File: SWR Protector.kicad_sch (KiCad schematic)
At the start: 28 parts, among them J1 Barrel_Jack, J2 Barrel_Jack, J3 transceiver, J4 antenna, J5 header, K2 ATX209, Q1 2N3904, T1 1:12, T2 1:12, U1 LM78L05_TO92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

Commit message: checkpoint changes working on V2.0
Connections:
- net +12V: now also U2.8 (V+)
- net +5V: no longer U2.8 (V+)
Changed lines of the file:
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@@
   (title_block
     (title "SWR Protector WA7GIL")
-    (date "2023-05-12")
-    (rev "v1.0")
+    (date "2023-05-27")
+    (rev "v1.1")
   )
   (junction (at 44.45 179.07) (diameter 0) (color 0 0 0 0)
@@
         (path "/5ddb5305-6e1d-4af3-a40a-20431dc1473c"
           (reference "#PWR06") (unit 1)
-        )
-      )
-    )
-  )
-  (symbol (lib_id "power:+5V") (at 129.54 161.29 0) (mirror x) (unit 1)
-    (in_bom yes) (on_board yes) (dnp no) (fields_autoplaced)
-    (property "Reference" "#PWR020" (at 129.54 157.48 0)
-      (effects (font (size 1.27 1.27)) hide)
-    )
-    (property "Value" "+5V" (at 129.54 166.37 0)
-      (effects (font (size 1.27 1.27)))
-    )
-    (property "Footprint" "" (at 129.54 161.29 0)
-      (effects (font (size 1.27 1.27)) hide)
-    )
-    (property "Datasheet" "" (at 129.54 161.29 0)
-      (effects (font (size 1.27 1.27)) hide)
-    )
-    (pin "1")
-    (instances
-      (project "SWR Protector"
-        (path "/46027dd5-036f-43c6-98e1-c4cfe473ecd7"
-          (reference "#PWR020") (unit 1)
-        )
-      )
-      (project "SWR Protector"
-        (path "/5ddb5305-6e1d-4af3-a40a-20431dc1473c"
-          (reference "#PWR020") (unit 1)
         )
       )
@@
         )
       )
+    )
+  )
+  (symbol (lib_id "power:+12V") (at 129.54 161.29 180) (unit 1)
+    (in_bom yes) (on_board yes) (dnp no) (fields_autoplaced)
+    (property "Reference" "#PWR031" (at 129.54 157.48 0)
+      (effects (font (size 1.27 1.27)) hide)
+    )
+    (property "Value" "+12V" (at 129.54 166.37 0)
+      (effects (font (size 1.27 1.27)))
+    )
+    (property "Footprint" "" (at 129.54 161.29 0)
+      (effects (font (size 1.27 1.27)) hide)
+    )
+    (property "Datasheet" "" (at 129.54 161.29 0)
+      (effects (font (size 1.27 1.27)) hide)
+    )
+    (pin "1")
+    (instances
+      (project "SWR Protector"
+        (path "/5ddb5305-6e1d-4af3-a40a-20431dc1473c"
+          (reference "#PWR031") (unit 1)
+        )
+      )

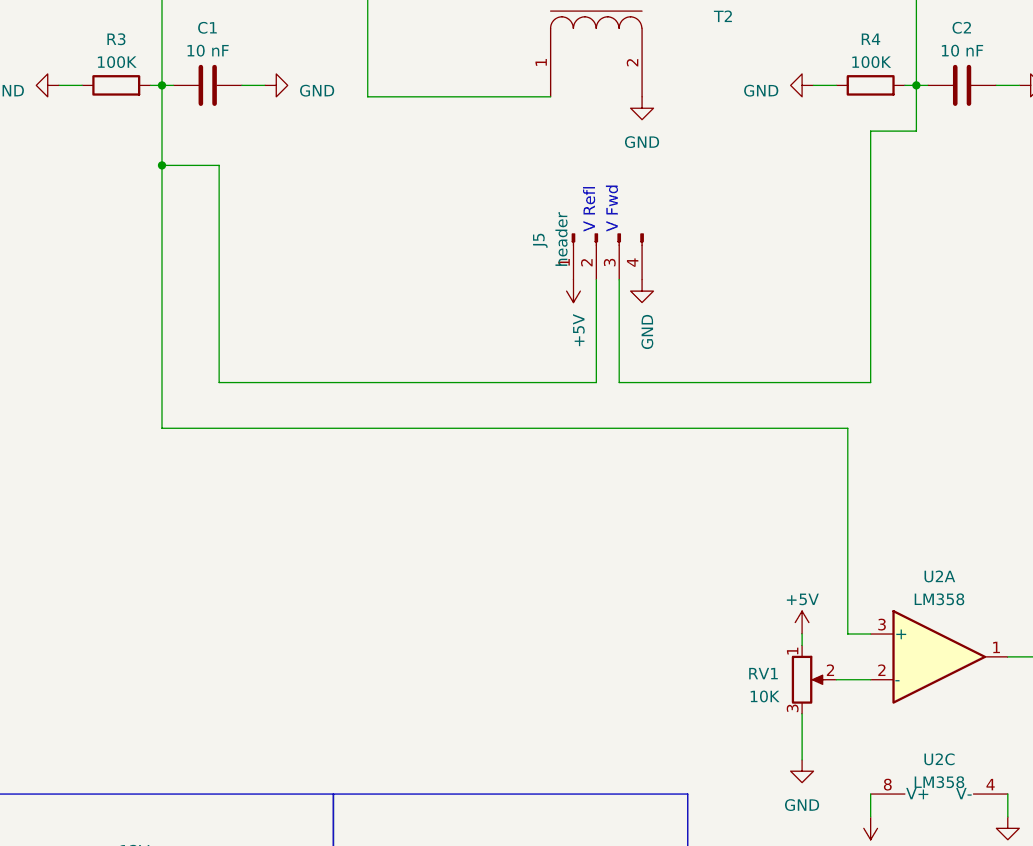
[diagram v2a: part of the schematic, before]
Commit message: v1.2 - added pins 2 & 3 from LM358 to header
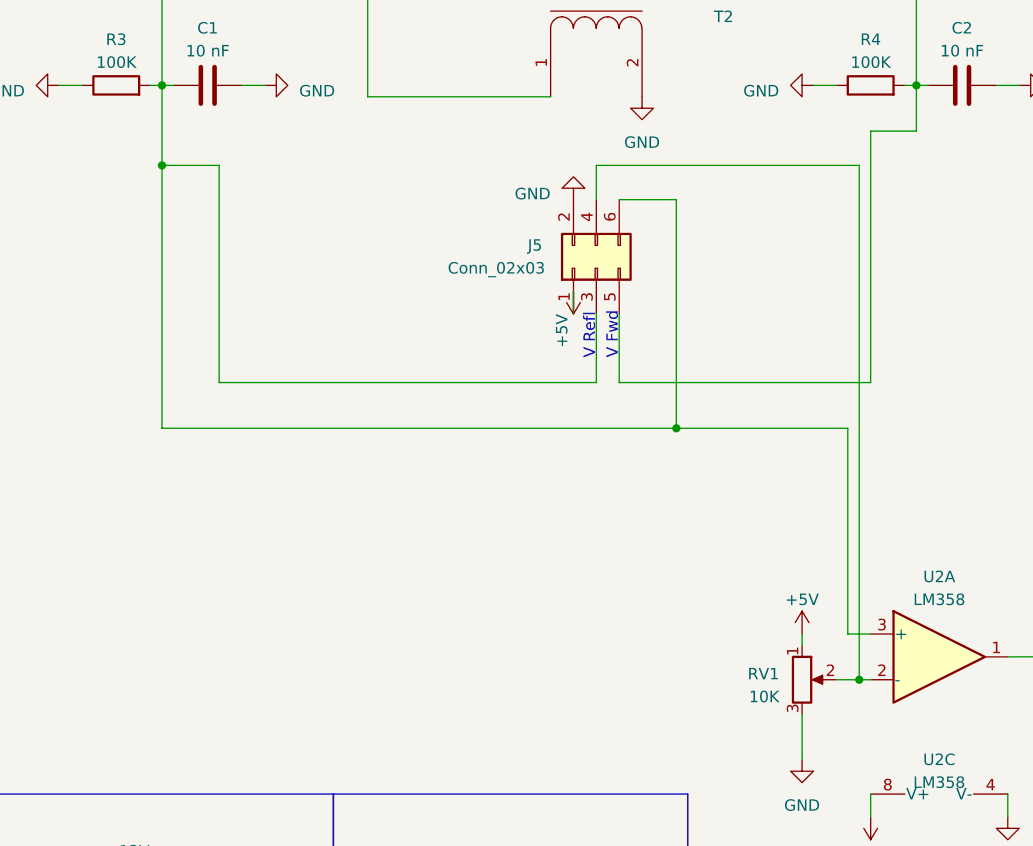
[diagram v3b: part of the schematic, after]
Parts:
- removed J5: header, Connector_PinHeader_2.54mm:PinHeader_1x04_P2.54mm_Vertical, symbol Connector:Conn_01x04_Pin
- added J5: Conn_02x03, Connector_PinHeader_2.54mm:PinHeader_2x03_P2.54mm_Vertical, symbol Connector_Generic:Conn_02x03_Odd_Even
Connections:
- net +5V: now also J5.1 (Pin_1)
- net GND: now also J5.2 (Pin_2)
- net at C2.1, D4.1 (K), R4.2: now also J5.5 (Pin_5)
- net at C1.1, D3.1 (K), R3.2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: now also J5.3 (Pin_3), J5.6 (Pin_6)
- net at RV1.2, U2.2 (-): now also J5.4 (Pin_4)

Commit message: checkpoint changes made late satuday that i cannot remember what i did
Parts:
- renumbered J5 to J3
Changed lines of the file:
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@@
       (project "SWR Protector"
         (path "/5ddb5305-6e1d-4af3-a40a-20431dc1473c"
-          (reference "#PWR022") (unit 1)
+          (reference "#PWR015") (unit 1)
         )
       )
@@
       (project "SWR Protector"
         (path "/5ddb5305-6e1d-4af3-a40a-20431dc1473c"
-          (reference "#PWR01") (unit 1)
+          (reference "#PWR04") (unit 1)
         )
       )
@@
       (project "SWR Protector"
         (path "/5ddb5305-6e1d-4af3-a40a-20431dc1473c"
-          (reference "C2") (unit 1)
+          (reference "C4") (unit 1)
         )
       )
@@
       (project "SWR Protector"
         (path "/5ddb5305-6e1d-4af3-a40a-20431dc1473c"
-          (reference "R1") (unit 1)
+          (reference "R5") (unit 1)
         )
       )
@@
       (project "SWR Protector"
         (path "/5ddb5305-6e1d-4af3-a40a-20431dc1473c"
-          (reference "#PWR012") (unit 1)
+          (reference "#PWR05") (unit 1)
         )
       )
@@
       (project "SWR Protector"
         (path "/5ddb5305-6e1d-4af3-a40a-20431dc1473c"
-          (reference "#PWR08") (unit 1)
+          (reference "#PWR017") (unit 1)
         )
       )
@@
       (project "SWR Protector"
         (path "/5ddb5305-6e1d-4af3-a40a-20431dc1473c"
-          (reference "D1") (unit 1)
+          (reference "D4") (unit 1)
         )
       )
@@
       (project "SWR Protector"
         (path "/5ddb5305-6e1d-4af3-a40a-20431dc1473c"
-          (reference "#PWR015") (unit 1)
+          (reference "#PWR022") (unit 1)
         )
       )
@@
       (project "SWR Protector"
         (path "/5ddb5305-6e1d-4af3-a40a-20431dc1473c"
-          (reference "R5") (unit 1)
+          (reference "R1") (unit 1)
         )
       )
@@
       (project "SWR Protector"
         (path "/5ddb5305-6e1d-4af3-a40a-20431dc1473c"
-          (reference "#PWR03") (unit 1)
+          (reference "#PWR024") (unit 1)
         )
       )
@@
       (project "SWR Protector"
         (path "/5ddb5305-6e1d-4af3-a40a-20431dc1473c"
-          (reference "#PWR09") (unit 1)
+          (reference "#PWR013") (unit 1)
         )
       )
@@
       (project "SWR Protector"
         (path "/5ddb5305-6e1d-4af3-a40a-20431dc1473c"
-          (reference "D3") (unit 1)
+          (reference "D1") (unit 1)
         )
       )
@@
       (project "SWR Protector"
         (path "/5ddb5305-6e1d-4af3-a40a-20431dc1473c"
-          (reference "#PWR018") (unit 1)
+          (reference "#PWR01") (unit 1)
         )
       )
@@
   (symbol (lib_id "Connector_Generic:Conn_02x03_Odd_Even") (at 99.06 100.33 90) (unit 1)
     (in_bom yes) (on_board yes) (dnp no)
-    (property "Reference" "J5" (at 91.44 97.79 90)
+    (property "Reference" "J3" (at 91.44 97.79 90)
       (effects (font (size 1.27 1.27)) (justify right))
     )
@@
       (project "SWR Protector"
         (path "/5ddb5305-6e1d-4af3-a40a-20431dc1473c"
-          (reference "J5") (unit 1)
+          (reference "J3") (unit 1)
         )
       )
@@
       (project "SWR Protector"
         (path "/5ddb5305-6e1d-4af3-a40a-20431dc1473c"
-          (reference "#PWR06") (unit 1)
+          (reference "#PWR03") (unit 1)
         )
       )
@@
       (project "SWR Protector"
         (path "/5ddb5305-6e1d-4af3-a40a-20431dc1473c"
-          (reference "D4") (unit 1)
+          (reference "D2") (unit 1)
         )
       )
@@
       (project "SWR Protector"
         (path "/5ddb5305-6e1d-4af3-a40a-20431dc1473c"
-          (reference "#PWR07") (unit 1)
+          (reference "#PWR027") (unit 1)
         )
       )
@@
       (project "SWR Protector"
         (path "/5ddb5305-6e1d-4af3-a40a-20431dc1473c"
-          (reference "J3") (unit 1)
+          (reference "J4") (unit 1)
         )
       )
@@
       (project "SWR Protector"
         (path "/5ddb5305-6e1d-4af3-a40a-20431dc1473c"
-          (reference "#PWR025") (unit 1)
+          (reference "#PWR029") (unit 1)
         )
       )
@@
       (project "SWR Protector"
         (path "/5ddb5305-6e1d-4af3-a40a-20431dc1473c"
-          (reference "J1") (unit 1)
+          (reference "J5") (unit 1)
         )
       )
@@
       (project "SWR Protector"
         (path "/5ddb5305-6e1d-4af3-a40a-20431dc1473c"
-          (reference "R6") (unit 1)
+          (reference "R4") (unit 1)
         )
       )
@@
       (project "SWR Protector"
         (path "/5ddb5305-6e1d-4af3-a40a-20431dc1473c"
-          (reference "J2") (unit 1)
+          (reference "J1") (unit 1)
         )
       )
@@
       (project "SWR Protector"
         (path "/5ddb5305-6e1d-4af3-a40a-20431dc1473c"
-          (reference "#PWR014") (unit 1)
+          (reference "#PWR018") (unit 1)
         )
       )
@@
       (project "SWR Protector"
         (path "/5ddb5305-6e1d-4af3-a40a-20431dc1473c"
-          (reference "#PWR05") (unit 1)
+          (reference "#PWR028") (unit 1)
         )
       )
@@
       (project "SWR Protector"
         (path "/5ddb5305-6e1d-4af3-a40a-20431dc1473c"
-          (reference "C4") (unit 1)
+          (reference "C2") (unit 1)
         )
       )
@@
       (project "SWR Protector"
         (path "/5ddb5305-6e1d-4af3-a40a-20431dc1473c"
-          (reference "R3") (unit 1)
+          (reference "R2") (unit 1)
         )
       )
@@
       (project "SWR Protector"
         (path "/5ddb5305-6e1d-4af3-a40a-20431dc1473c"
-          (reference "#PWR030") (unit 1)
+          (reference "#PWR011") (unit 1)
         )
       )
@@
       (project "SWR Protector"
         (path "/5ddb5305-6e1d-4af3-a40a-20431dc1473c"
-          (reference "#PWR021") (unit 1)
+          (reference "#PWR07") (unit 1)
         )
       )
@@
       (project "SWR Protector"
         (path "/5ddb5305-6e1d-4af3-a40a-20431dc1473c"
-          (reference "R2") (unit 1)
+          (reference "R6") (unit 1)
         )
       )
@@
       (project "SWR Protector"
         (path "/5ddb5305-6e1d-4af3-a40a-20431dc1473c"
-          (reference "D2") (unit 1)
+          (reference "D3") (unit 1)
         )
       )
@@
       (project "SWR Protector"
         (path "/5ddb5305-6e1d-4af3-a40a-20431dc1473c"
-          (reference "#PWR017") (unit 1)
+          (reference "#PWR023") (unit 1)
         )
       )
@@
       (project "SWR Protector"
         (path "/5ddb5305-6e1d-4af3-a40a-20431dc1473c"
-          (reference "#PWR027") (unit 1)
+          (reference "#PWR014") (unit 1)
         )
       )
@@
       (project "SWR Protector"
         (path "/5ddb5305-6e1d-4af3-a40a-20431dc1473c"
-          (reference "J4") (unit 1)
+          (reference "J2") (unit 1)
         )
       )
@@
       (project "SWR Protector"
         (path "/5ddb5305-6e1d-4af3-a40a-20431dc1473c"
-          (reference "#PWR024") (unit 1)
+          (reference "#PWR016") (unit 1)
         )
       )
@@
       (project "SWR Protector"
         (path "/5ddb5305-6e1d-4af3-a40a-20431dc1473c"
-          (reference "K2") (unit 1)
+          (reference "K1") (unit 1)
         )
       )
@@
       (project "SWR Protector"
         (path "/5ddb5305-6e1d-4af3-a40a-20431dc1473c"
-          (reference "#PWR04") (unit 1)
+          (reference "#PWR026") (unit 1)
         )
       )
@@
       (project "SWR Protector"
         (path "/5ddb5305-6e1d-4af3-a40a-20431dc1473c"
-          (reference "#PWR028") (unit 1)
+          (reference "#PWR09") (unit 1)
         )
       )
@@
   (symbol (lib_id "power:+12V") (at 129.54 161.29 180) (unit 1)
     (in_bom yes) (on_board yes) (dnp no) (fields_autoplaced)
-    (property "Reference" "#PWR031" (at 129.54 157.48 0)
+    (property "Reference" "#PWR019" (at 129.54 157.48 0)
       (effects (font (size 1.27 1.27)) hide)
     )
@@
       (project "SWR Protector"
         (path "/5ddb5305-6e1d-4af3-a40a-20431dc1473c"
-          (reference "#PWR031") (unit 1)
+          (reference "#PWR019") (unit 1)
         )
       )
@@
       (project "SWR Protector"
         (path "/5ddb5305-6e1d-4af3-a40a-20431dc1473c"
-          (reference "#PWR013") (unit 1)
+          (reference "#PWR02") (unit 1)
         )
       )
@@
       (project "SWR Protector"
         (path "/5ddb5305-6e1d-4af3-a40a-20431dc1473c"
-          (reference "#PWR011") (unit 1)
+          (reference "#PWR08") (unit 1)
         )
       )
@@
       (project "SWR Protector"
         (path "/5ddb5305-6e1d-4af3-a40a-20431dc1473c"
-          (reference "#PWR016") (unit 1)
+          (reference "#PWR06") (unit 1)
         )
       )
@@
       (project "SWR Protector"
         (path "/5ddb5305-6e1d-4af3-a40a-20431dc1473c"
-          (reference "#PWR019") (unit 1)
+          (reference "#PWR021") (unit 1)
         )
       )
@@
       (project "SWR Protector"
         (path "/5ddb5305-6e1d-4af3-a40a-20431dc1473c"
-          (reference "#PWR029") (unit 1)
+          (reference "#PWR012") (unit 1)
         )
       )
@@
       (project "SWR Protector"
         (path "/5ddb5305-6e1d-4af3-a40a-20431dc1473c"
-          (reference "#PWR023") (unit 1)
+          (reference "#PWR025") (unit 1)
         )
       )
@@
       (project "SWR Protector"
         (path "/5ddb5305-6e1d-4af3-a40a-20431dc1473c"
-          (reference "#PWR02") (unit 1)
+          (reference "#PWR010") (unit 1)
         )
       )
@@
       (project "SWR Protector"
         (path "/5ddb5305-6e1d-4af3-a40a-20431dc1473c"
-          (reference "#PWR010") (unit 1)
+          (reference "#PWR020") (unit 1)
         )
       )
@@
       (project "SWR Protector"
         (path "/5ddb5305-6e1d-4af3-a40a-20431dc1473c"
-          (reference "R4") (unit 1)
+          (reference "R3") (unit 1)
         )
       )
@@
       (project "SWR Protector"
         (path "/5ddb5305-6e1d-4af3-a40a-20431dc1473c"
-          (reference "#PWR026") (unit 1)
-        )
-      )
+          (reference "#PWR030") (unit 1)
+        )
+      )

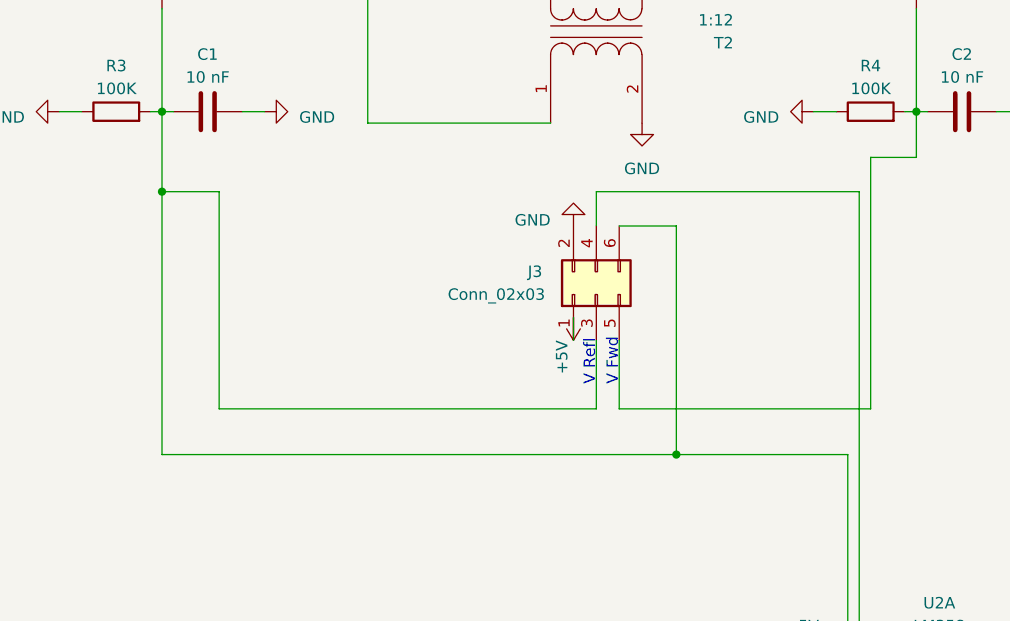
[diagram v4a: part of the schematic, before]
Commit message: Removed pin 6 on header.  Fine tune footprint for Q1. Realizing pin 6 on header just duplicated the VReflected voltage already on pin 3, I made pin 6 NC. Fiddled with footprint for Q1 to try to remove "Silkscreen clipped by solder mask" warnings.
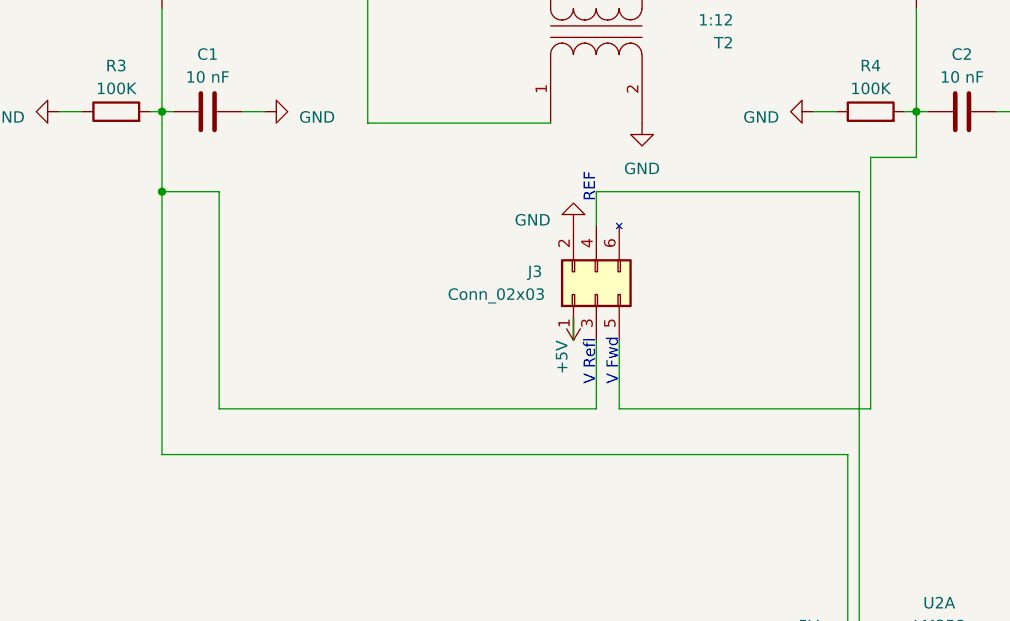
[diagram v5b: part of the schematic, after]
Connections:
- net at C1.1, D3.1 (K), J3.3 (Pin_3)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: no longer J3.6 (Pin_6)
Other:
- note added: "REF"
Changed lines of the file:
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@@
   (title_block
     (title "SWR Protector WA7GIL")
-    (date "2023-05-27")
-    (rev "v1.2")
+    (date "2023-05-28")
+    (rev "v1.3")
   )
   (junction (at 44.45 179.07) (diameter 0) (color 0 0 0 0)
-  )
-  (junction (at 107.95 118.11) (diameter 0) (color 0 0 0 0)
   )
   (junction (at 181.61 138.43) (diameter 0) (color 0 0 0 0)
@@
     (stroke (width 0) (type default))
   )
-  (wire (pts (xy 107.95 92.71) (xy 107.95 118.11))
-    (stroke (width 0) (type default))
-  )
-  (wire (pts (xy 50.8 118.11) (xy 107.95 118.11))
+  (wire (pts (xy 50.8 118.11) (xy 127 118.11))
     (stroke (width 0) (type default))
   )
@@
     (stroke (width 0) (type default))
   )
-  (wire (pts (xy 107.95 118.11) (xy 127 118.11))
-    (stroke (width 0) (type default))
-  )
   (wire (pts (xy 59.69 80.01) (xy 62.23 80.01))
     (stroke (width 0) (type default))
@@
     (stroke (width 0) (type default))
   )
-  (wire (pts (xy 101.6 92.71) (xy 107.95 92.71))
-    (stroke (width 0) (type default))
-  )
   (wire (pts (xy 168.91 138.43) (xy 181.61 138.43))
     (stroke (width 0) (type default))
@@
     (effects (font (size 1.27 1.27)) (justify left bottom))
   )
+  (text "REF" (at 99.06 90.17 90)
+    (effects (font (size 1.27 1.27)) (justify left bottom))
+  )
